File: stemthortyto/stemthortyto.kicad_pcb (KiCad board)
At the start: 8 copper layers, 60 parts, among them IC1 E22-900M22S, Q1 BCV29, U2 ADXL343, U3 RK3588S, U4 K4UCE3Q4AB-MGCL, U5 FEMDRW032G-88A19

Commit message: Add files via upload
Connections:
- U4 pad D10: WCK1PA -> DQS1PA
- U4 pad D3: WCK0PA -> DQS0PA
- U4 pad E10: WCK1NA -> DQS1NA
- U4 pad E3: WCK0NA -> DQS0NA
- U4 pad V10: WCK1NB -> DQS1NB
- U4 pad V3: WCK0NB -> DQS0NB
- U4 pad W10: WCK1PB -> DQS1PB
- U4 pad W3: WCK0PB -> DQS0PB
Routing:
- net A5B: track 0.00 -> 46.4 mm, vias 1 -> 3
- net DQS1NA: track 0.00 -> 13.8 mm, vias 0 -> 2
- net WCK1NA: track 13.3 -> 0.00 mm, vias 2 -> 0
- net DQS1PA: track 0.00 -> 12.8 mm, vias 0 -> 2
- net WCK0NB: track 12.4 -> 0.00 mm, vias 2 -> 0
- net DQS0NB: track 0.00 -> 12.2 mm, vias 0 -> 2
- net WCK0PB: track 11.8 -> 0.00 mm, vias 2 -> 0
- net DQS0PB: track 0.00 -> 11.6 mm, vias 0 -> 2
- net DQS1NB: track 0.00 -> 11.4 mm, vias 0 -> 2
- net DQS1PB: track 0.00 -> 11.0 mm, vias 0 -> 2
- net DQ0B: track 6.85 -> 8.19 mm
- net DQ1B: track 8.28 -> 9.57 mm
- net DQ8A: track 18.0 -> 18.7 mm
- net DM0B: track 9.01 -> 9.67 mm
- net ZQ0: vias 19 -> 18
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
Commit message: Finished wiring for eMMC and DRAM
The signals have been completed however the power is yet to be resolved.
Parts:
- moved C35 0.07 mm to (114.9, 72.1), turned to 180 degrees
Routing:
- net DAT7: track 0.35 -> 20.5 mm
- net EMCIO: track 6.57 -> 25.4 mm
- net DAT6: track 0.35 -> 19.1 mm
- net DAT2: track 0.35 -> 16.4 mm
- net DAT0: track 1.14 -> 15.5 mm
- net DAT5: track 0.35 -> 14.7 mm
- net DAT1: track 0.35 -> 14.7 mm
- net DAT4: track 0.35 -> 13.2 mm
- net DAT3: track 0.35 -> 12.5 mm
- net Net-(U5-DS): track 0.99 -> 11.7 mm
- net Net-(U5-RSTN): track 0.98 -> 9.95 mm
- net RST: track 0.76 -> 8.62 mm
- net DQS0PA: track 0.00 -> 6.65 mm, vias 0 -> 2
- net CMD: track 1.07 -> 7.47 mm
- net DQS0NA: track 0.00 -> 6.14 mm, vias 0 -> 2

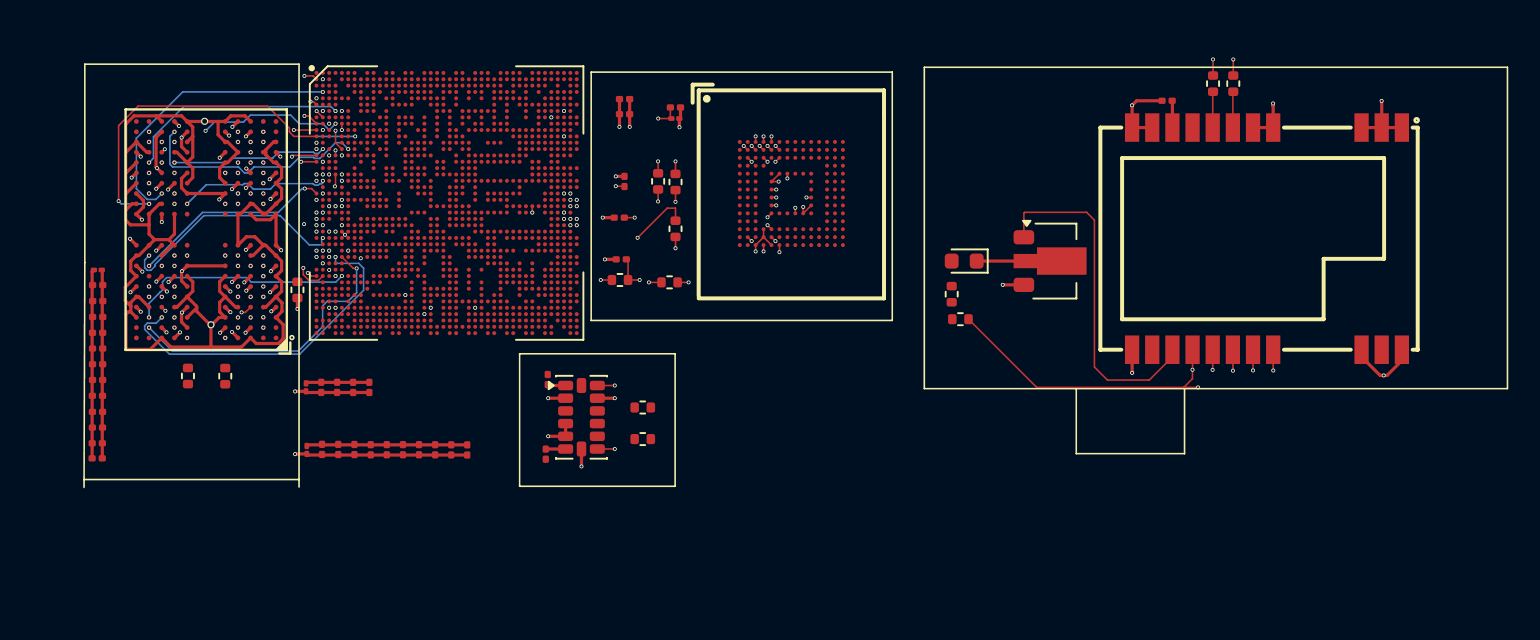
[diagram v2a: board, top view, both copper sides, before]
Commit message: GND Plane
added a gnd plane and also wired the 1.1v for DRAM
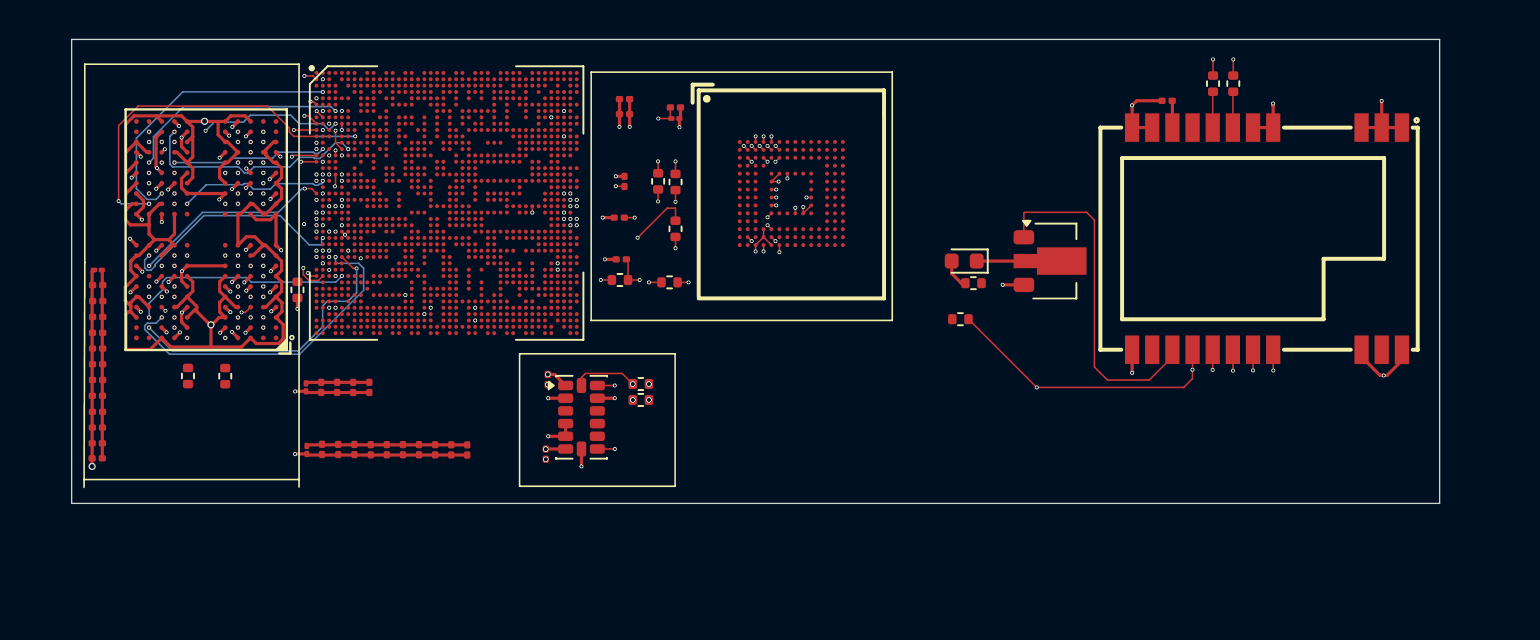
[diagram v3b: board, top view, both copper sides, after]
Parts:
- moved R2 3.47 mm to (116.2, 82.6), turned to 180 degrees
- moved R4 1.54 mm to (137.2, 76.2), turned to 180 degrees
- moved R1 0.49 mm to (116.2, 83.6), turned to 180 degrees
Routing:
- net +1V1: track 32.8 -> 80.6 mm, vias 17 -> 18
- net ACCLINT: track 1.10 -> 19.2 mm, vias 1 -> 2
- net +3.3V: track 9.04 -> 23.1 mm, vias 4 -> 8
- net SCLACCL: track 0.00 -> 13.7 mm, vias 0 -> 2
- net LoRaRST: track 80.9 -> 69.9 mm
- net SDAACCL: track 1.10 -> 11.5 mm, vias 1 -> 3
- net Net-(D1-A): track 0.00 -> 1.90 mm
- net GND: vias 31 -> 33
- added copper zone on In1.Cu, net GND
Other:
- board outline added: 86.2 x 29.2 mm

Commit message: Pwr.rout.comp.formmcddr, curr. using a barrel jack
Updated the board so that the power bus is ready for LPDDR and the eMMC is connected fully. Currently using a TO package linear regulator 3.3V@7.2A The eMMC data traces have also been length matched to +-4mm from each other, seeing as we're operating that at low R/W speeds anyway, shouldn't be a problem and is an upgrade from +-12mm.
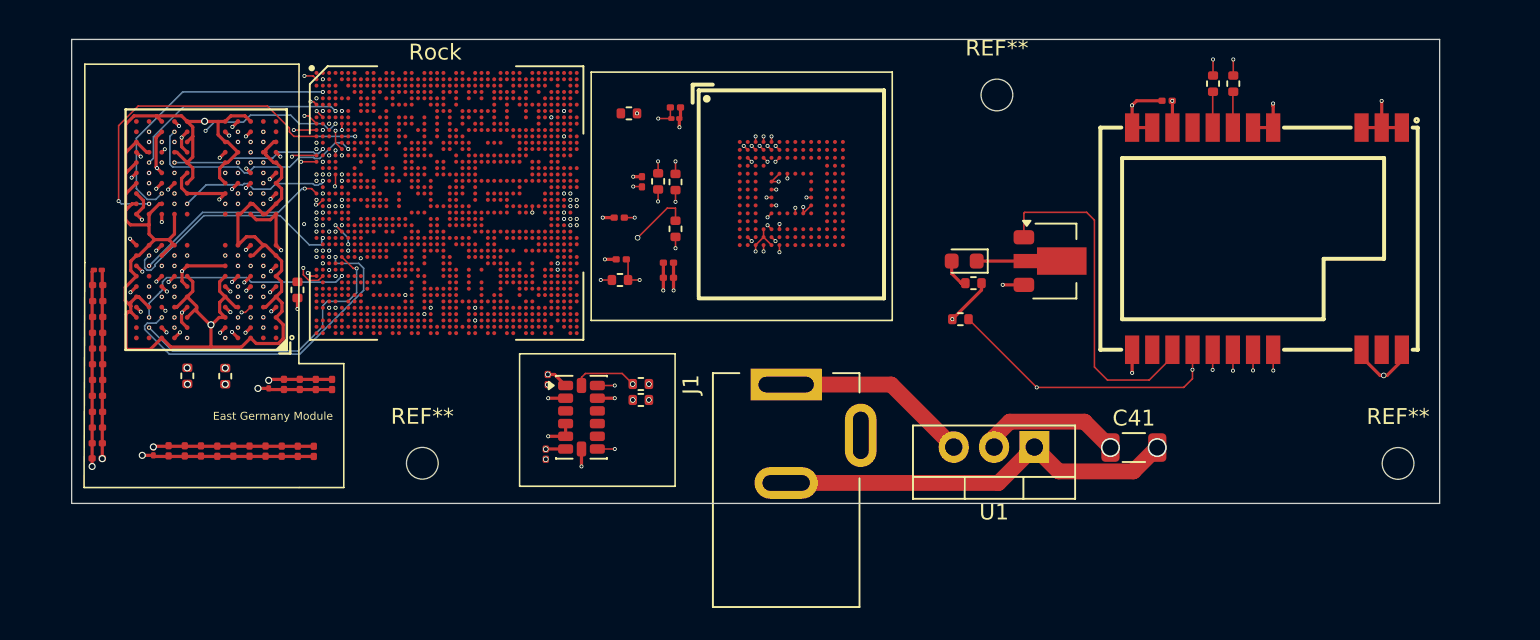
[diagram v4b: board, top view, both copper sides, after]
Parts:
- added C41: 22μF, Capacitor_SMD:C_1206_3216Metric, F.Cu at (147.3, 86.6)
- added J1: Jack-DC, Connector_BarrelJack:BarrelJack_Kycon_KLDX-0202-xC_Horizontal, F.Cu at (125.4, 82.6)
- added REF**: MountingHole_2mm, MountingHole:MountingHole_2mm, F.Cu at (164.0, 87.6)
- added REF**: MountingHole_2mm, MountingHole:MountingHole_2mm, F.Cu at (138.7, 64.4)
- added REF**: MountingHole_2mm, MountingHole:MountingHole_2mm, F.Cu at (102.5, 87.6)
- added U1: LT1585-3.3, Package_TO_SOT_THT:TO-220-3_Vertical, F.Cu at (141.0, 86.6)
- moved R14 11.0 mm to (115.5, 65.5)
- moved C37 10.7 mm to (118.0, 75.9)
- moved C36 10.7 mm to (118.0, 75.0)
- moved C10 9.67 mm to (86.5, 86.8)
- moved C12 9.67 mm to (88.5, 86.8)
- moved C13 9.67 mm to (89.5, 86.8)
- moved C7 9.67 mm to (93.6, 86.8)
- moved C8 9.67 mm to (94.6, 86.8)
- moved C11 9.67 mm to (87.5, 86.8)
- moved C14 9.67 mm to (90.6, 86.8)
- moved C15 9.67 mm to (85.5, 86.8)
- moved C5 9.67 mm to (91.6, 86.8)
- moved C6 9.67 mm to (92.6, 86.8)
- moved C9 9.67 mm to (95.6, 86.8)
- moved C29 2.36 mm to (93.8, 82.6)
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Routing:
- net +3.3V: track 23.1 -> 115.0 mm, vias 8 -> 11
- net +1V8: track 8.91 -> 47.9 mm
- net Net-(U1-GND): track 0.00 -> 25.6 mm, vias 0 -> 1
- net EMCIO: track 25.4 -> 43.9 mm
- net Net-(U1-VI): track 0.00 -> 12.2 mm
- net Net-(U5-CLK): track 2.13 -> 13.2 mm, vias 1 -> 2
- net Net-(U5-VDDI): track 0.88 -> 11.6 mm
- net CKA: track 0.00 -> 9.96 mm, vias 1 -> 2
- net ZQ0: track 22.8 -> 32.0 mm, vias 18 -> 20
- net DAT4: track 13.2 -> 18.9 mm
- net CLKOUT: track 0.70 -> 6.14 mm
- net DAT5: track 14.7 -> 19.1 mm
- net Net-(U5-DS): track 11.7 -> 15.9 mm
- net LoRaMOSI: track 56.9 -> 60.2 mm
- net DAT3: track 12.5 -> 15.7 mm
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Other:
- board text added: "East Germany Module"
- board text added: "Rock"
- board text added: "TODO, CKA is not connected."

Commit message: Add files via upload
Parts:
- C33, C34: moved to B.Cu
- moved C26 21.4 mm to (102.4, 82.1), turned to -90 degrees
- moved C28 20.2 mm to (101.4, 82.1), turned to -90 degrees
- moved C19 19.0 mm to (100.4, 82.1), turned to -90 degrees
- moved C20 17.8 mm to (99.4, 82.1), turned to -90 degrees
- moved C21 16.6 mm to (98.4, 82.1), turned to -90 degrees
- moved C22 15.5 mm to (97.4, 82.1), turned to -90 degrees
- moved C23 14.4 mm to (96.4, 82.1), turned to -90 degrees
- moved C24 13.4 mm to (95.4, 82.1), turned to -90 degrees
- moved C25 12.5 mm to (94.4, 82.1), turned to -90 degrees
- moved C27 11.6 mm to (93.4, 82.1), turned to -90 degrees
- moved R10 11.4 mm to (103.6, 83.7), turned to 0 degrees
- moved C16 10.9 mm to (92.4, 82.1), turned to -90 degrees
- moved C17 10.4 mm to (91.4, 82.1), turned to -90 degrees
- moved C34 10.1 mm to (125.0, 72.9), turned to -90 degrees
- moved C18 9.97 mm to (90.5, 82.1), turned to -90 degrees
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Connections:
- net CKA renamed CKA_P
- net CKB renamed CKB_P
- net CKBA renamed CKA_N
- net CKBB renamed CKB_N
- U3 pad AA5: DQ1B -> DQ6B
- U3 pad AB3: DQ3A -> DQ5A
- U3 pad AB4: DQ1A -> DQ4A
- U3 pad AB5: DQ4A -> DQ3A
- U3 pad AE5: DQ5A -> DQ2A
- U3 pad AF3: DQ7A -> DQ1A
- U3 pad AF4: DQ14A -> DQ10A
- U3 pad AF5: DQ15A -> DQ11A
- U3 pad AJ1: DQ2A -> DQ7A
- U3 pad AJ3: DQ12A -> DQ13A
- U3 pad AJ6: DQ11A -> DQ12A
- U3 pad AK3: DQ13A -> DQ14A
- U3 pad AK5: DQ8A -> DQ15A
- U3 pad AN4: DQ10A -> DQ9A
- U3 pad AN5: DQ9A -> DQ8A
- U3 pad G4: DQ10B -> DQ9B
- U3 pad J3: DQ9B -> DQ13B
- U3 pad J4: DQ11B -> DQ15B
- U3 pad N2: DQ13B -> DQ12B
- U3 pad N5: DQ12B -> DQ11B
- U3 pad N6: DQ15B -> DQ10B
- U3 pad P3: DQ5B -> DQ0B
- U3 pad P4: DQ4B -> DQ3B
- U3 pad U3: DQ0B -> DQ4B
- U3 pad U4: DQ6B -> DQ5B
- U3 pad U5: DQ3B -> DQ1B
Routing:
- net GND: track 156.4 -> 54.3 mm, vias 36 -> 25
- net +1V1: track 80.7 -> 12.4 mm, vias 18 -> 1
- net +1V8: track 47.9 -> 4.70 mm, vias 9 -> 1
- net EMCIO: track 43.9 -> 15.3 mm, vias 7 -> 4
- net A5B: track 46.4 -> 19.8 mm, vias 3 -> 2
- net +3.3V: track 115.0 -> 95.1 mm, vias 11 -> 10
- net DQ2B: track 3.70 -> 20.9 mm
- net DQ2A: track 4.71 -> 21.5 mm
- net CKE0A: track 5.49 -> 21.2 mm
- net DQ3B: track 5.24 -> 20.9 mm
- net Net-(U5-DS): track 15.9 -> 0.31 mm, vias 2 -> 1
- net A1B: track 4.86 -> 20.4 mm
- net DQS0NA: track 6.14 -> 21.0 mm
- net A1A: track 5.22 -> 20.1 mm
- net DQS0PA: track 6.65 -> 21.0 mm
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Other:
- board size 86.2 x 29.2 mm -> 88.7 x 29.2 mm

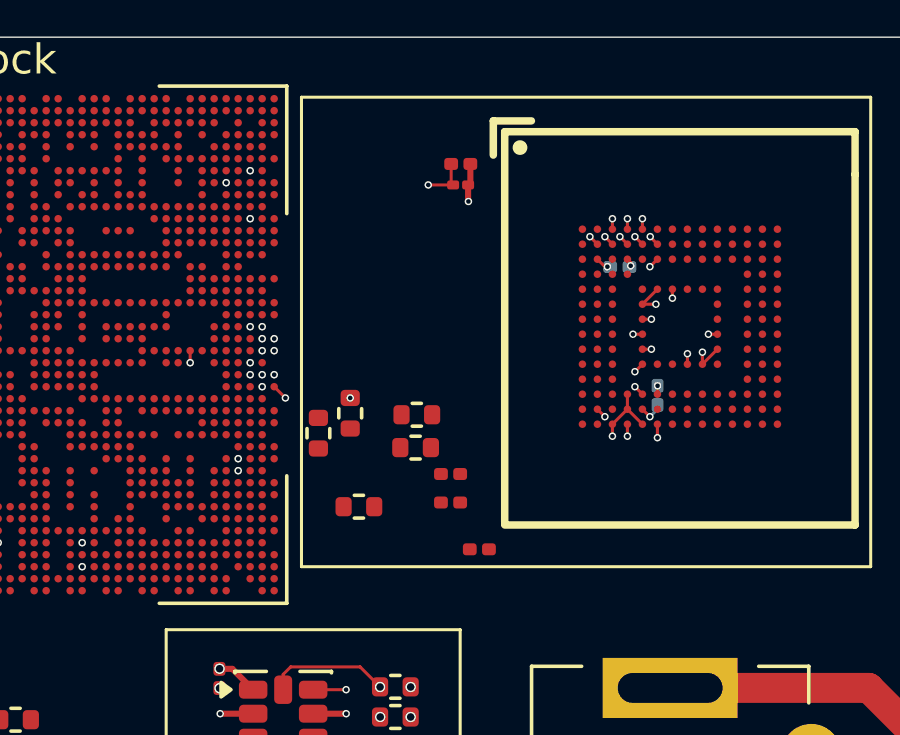
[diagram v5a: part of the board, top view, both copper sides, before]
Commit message: Update eMMC
Updated eMMC routing removed certain resistors (0 ohm, used for jumping/ troubleshooting probably but harmful to the design)
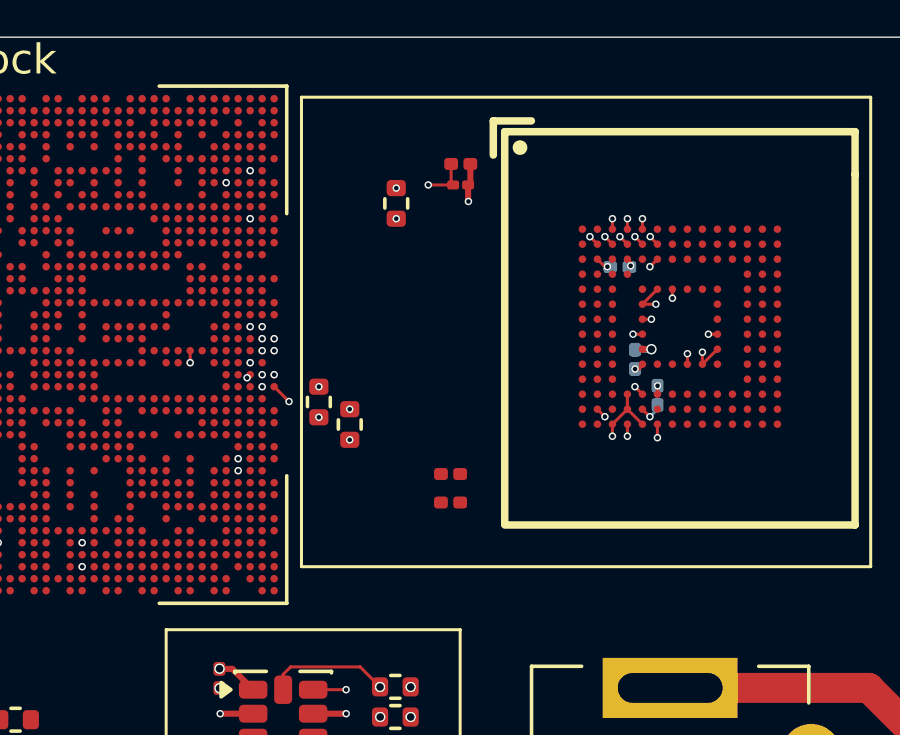
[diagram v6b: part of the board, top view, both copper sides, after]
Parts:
- removed R13: R_Small, Resistor_SMD:R_0402_1005Metric
- removed R14: 0, Resistor_SMD:R_0402_1005Metric
- C33: value 1μf -> 2.2μf
- C35: moved to B.Cu
- moved C35 8.19 mm to (124.2, 71.7), turned to 90 degrees
- moved R12 7.08 mm to (116.3, 66.5), turned to -90 degrees
- moved R9 3.57 mm to (113.7, 73.1), turned to 90 degrees
- moved R11 0.38 mm to (114.7, 73.9)
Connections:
- C34 pad 1: Net-(U5-CLK) -> CLKOUT
- C35 pad 1: Net-(U5-RSTN) -> RST
- U5 pad H5: Net-(U5-DS) -> DATASTROBE
- U5 pad K5: Net-(U5-RSTN) -> RST
- U5 pad M6: Net-(U5-CLK) -> CLKOUT
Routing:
- net RST: track 0.00 -> 17.3 mm, vias 1 -> 3
- net CLKOUT: track 0.00 -> 17.3 mm, vias 1 -> 2
- net DATASTROBE: track 0.00 -> 17.2 mm, vias 1 -> 2
- net CMD: track 12.7 -> 20.1 mm
- net EMCIO: track 15.3 -> 21.7 mm, vias 4 -> 7
- net DAT3: track 12.3 -> 17.3 mm
- net DAT4: track 13.0 -> 17.2 mm
- net DAT0: track 13.6 -> 17.2 mm, vias 2 -> 3
- net DAT5: track 13.8 -> 17.3 mm
- net DAT1: track 14.7 -> 17.4 mm
- net DAT2: track 14.7 -> 17.3 mm
- net DAT6: track 15.0 -> 17.2 mm
- net DAT7: track 15.4 -> 17.3 mm
- net GND: track 54.3 -> 54.8 mm
- net Net-(U5-RSTN): track 0.35 -> 0.00 mm, vias 1 -> 0
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
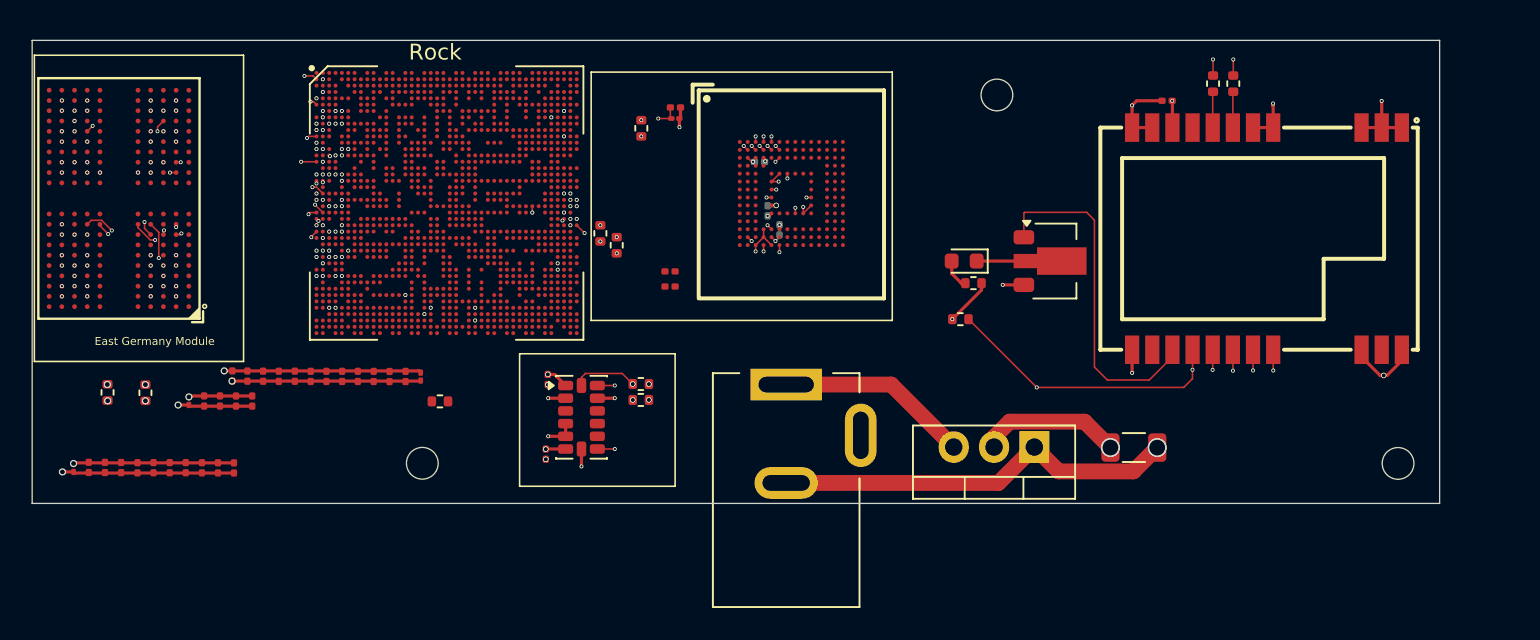
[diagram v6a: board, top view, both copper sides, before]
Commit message: decoupling and power plane
Mostly did some cleaning up , for some reason a bunch of pins were connected at sharp angles and also for some reason the GND plane was connected to 3.3V not GND which is very odd.
![[Pasted image 20260919230057.png]]
routed and connected a decoupling capacitor to every pair along with one bulk capacitor for the whole group of them.
![[Pasted image 20260919230646.png]]
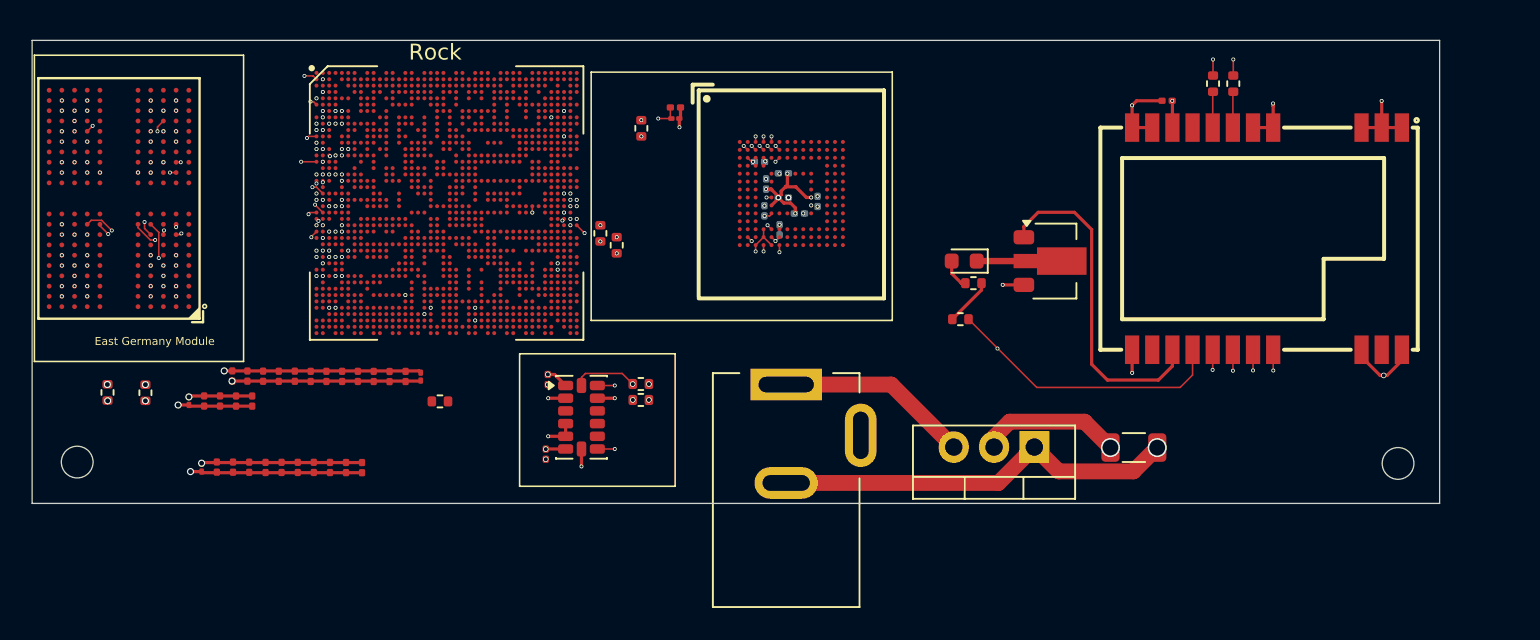
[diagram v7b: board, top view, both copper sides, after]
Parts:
- removed the REF** at (138.7, 64.4)
- added C42: 0.1μF, Capacitor_SMD:C_0201_0603Metric, B.Cu at (127.4, 71.1)
- added C43: 0.1μF, Capacitor_SMD:C_0201_0603Metric, B.Cu at (125.2, 69.3)
- added C45: 0.1μF, Capacitor_SMD:C_0201_0603Metric, B.Cu at (124.1, 70.0)
- C33: value 2.2μf -> 1μf
- C36, C37: moved to B.Cu
- moved REF** 21.8 mm to (80.7, 87.5)
- moved C37 9.36 mm to (126.2, 71.9), turned to 180 degrees
- moved C36 8.52 mm to (125.2, 70.9), turned to 180 degrees
- moved C11 8.07 mm to (90.5, 87.8)
- moved C12 8.07 mm to (91.6, 87.8)
- moved C13 8.07 mm to (92.6, 87.9)
- moved C15 8.07 mm to (88.6, 87.9)
- moved C5 8.07 mm to (94.6, 87.9)
- moved C7 8.07 mm to (96.7, 87.9)
- moved C9 8.07 mm to (98.7, 87.9)
- moved C10 8.07 mm to (89.5, 87.8)
- moved C14 8.07 mm to (93.6, 87.9)
- moved C6 8.07 mm to (95.6, 87.9)
- moved C8 8.07 mm to (97.7, 87.9)
- moved C35 0.20 mm to (124.0, 71.7)
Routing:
- net +3.3V: track 95.1 -> 30.9 mm, vias 10 -> 13
- net GND: track 54.8 -> 60.5 mm, vias 25 -> 27
- net LoRaBUSY: track 21.8 -> 21.2 mm
- net LoRaRST: track 70.6 -> 70.5 mm, vias 3 -> 2
